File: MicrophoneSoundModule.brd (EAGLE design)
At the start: 22.9 x 17.8 mm, 23 parts, among them IC1 TLC272 TSSOP8

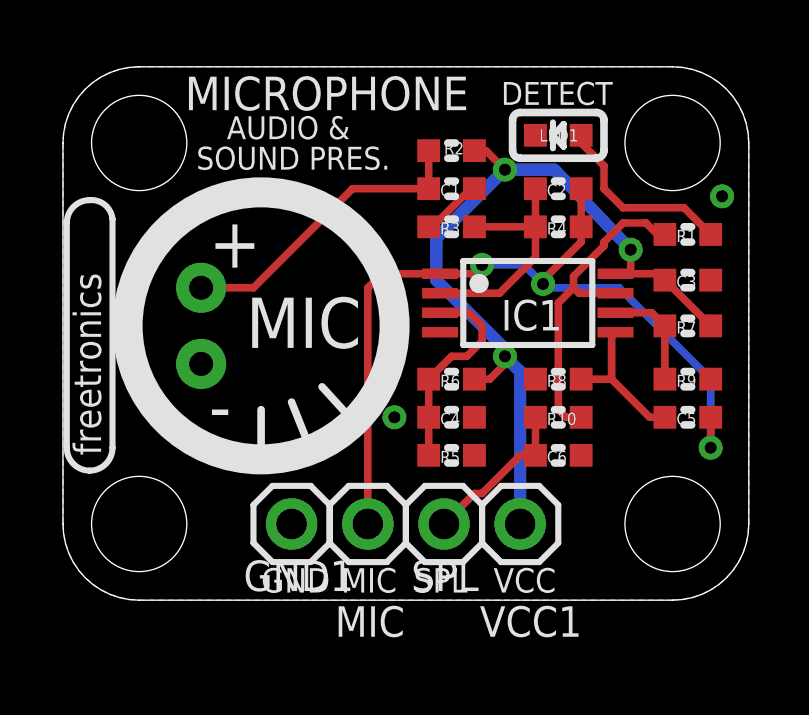
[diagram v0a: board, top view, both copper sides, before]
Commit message: Reorient AC decoupling capacitors to reduce noise
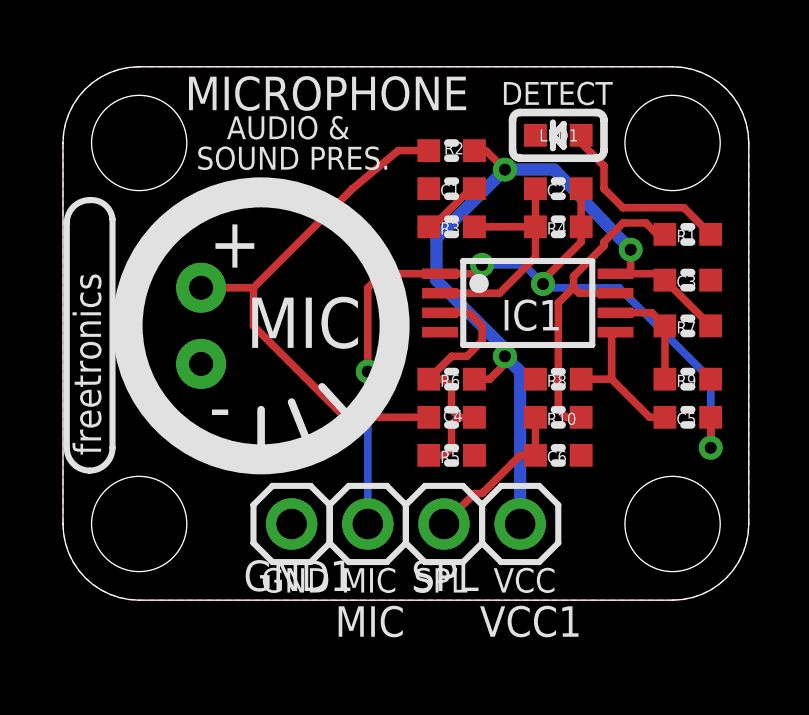
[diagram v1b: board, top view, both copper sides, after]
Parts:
- C4: value 1uF 10V -> 4.7uF 10V
- turned C4 to 0 degrees
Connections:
- net GND: now also C1.1; no longer C4.1
- net N$2: now also C4.1; no longer C1.1
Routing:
- net N$2: track 10.2 -> 17.8 mm
- net N$8: track 6.93 -> 8.88 mm
- net N$6: vias 3 -> 4
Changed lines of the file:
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@@
 <layer number="23" name="tOrigins" color="15" fill="1" visible="yes" active="yes"/>
 <layer number="24" name="bOrigins" color="15" fill="1" visible="yes" active="yes"/>
-<layer number="25" name="tNames" color="7" fill="1" visible="no" active="yes"/>
+<layer number="25" name="tNames" color="7" fill="1" visible="yes" active="yes"/>
 <layer number="26" name="bNames" color="7" fill="1" visible="no" active="yes"/>
 <layer number="27" name="tValues" color="7" fill="1" visible="no" active="yes"/>
@@
 <attribute name="VALUE" x="11.938" y="6.4008" size="0.4064" layer="27" font="vector"/>
 </element>
-<element name="C4" library="freetronics-master-v1" package="0603" value="1uF 10V" x="12.954" y="6.096" smashed="yes" rot="R180">
-<attribute name="NAME" x="12.573" y="5.842" size="0.4064" layer="25" font="vector"/>
-<attribute name="VALUE" x="13.97" y="7.0612" size="0.4064" layer="27" font="vector" rot="R180"/>
+<element name="C4" library="freetronics-master-v1" package="0603" value="4.7uF 10V" x="12.954" y="6.096" smashed="yes">
+<attribute name="NAME" x="13.335" y="6.35" size="0.4064" layer="25" font="vector" rot="R180"/>
+<attribute name="VALUE" x="11.938" y="5.1308" size="0.4064" layer="27" font="vector"/>
 </element>
 <element name="C5" library="freetronics-master-v1" package="0603" value="100nF" x="20.828" y="6.096" smashed="yes" rot="R180">
@@
 <contactref element="MIC1" pad="GND"/>
 <contactref element="R5" pad="1"/>
-<contactref element="C4" pad="1"/>
 <contactref element="R8" pad="1"/>
 <contactref element="R9" pad="1"/>
 <contactref element="C6" pad="1"/>
 <contactref element="GND1" pad="1"/>
-<via x="11.049" y="6.096" extent="1-16" drill="0.4"/>
-<via x="21.971" y="13.462" extent="1-16" drill="0.4"/>
 <polygon width="0.2032" layer="16" orphans="yes">
 <vertex x="2.54" y="17.78" curve="90"/>
@@
 <vertex x="2.54" y="17.78" curve="90"/>
 </polygon>
+<contactref element="C1" pad="1"/>
 </signal>
 <signal name="VCC">
@@
 <contactref element="IC1" pad="8"/>
 <contactref element="C3" pad="1"/>
-<contactref element="R6" pad="2"/>
 <contactref element="R7" pad="2"/>
 <contactref element="VCC1" pad="1"/>
@@
 <wire x1="14.732" y1="8.128" x2="14.732" y2="7.874" width="0.254" layer="1"/>
 <wire x1="14.732" y1="7.874" x2="14.224" y2="7.366" width="0.254" layer="1"/>
-<wire x1="14.224" y1="7.366" x2="13.716" y2="7.366" width="0.254" layer="1"/>
 <via x="18.923" y="11.684" extent="1-16" drill="0.4"/>
 <via x="14.732" y="14.351" extent="1-16" drill="0.4"/>
 <via x="14.732" y="8.128" extent="1-16" drill="0.4"/>
+<contactref element="R6" pad="2"/>
+<wire x1="14.224" y1="7.366" x2="13.716" y2="7.366" width="0.254" layer="1"/>
 </signal>
 <signal name="N$1">
@@
 <signal name="N$2">
 <contactref element="MIC1" pad="POS"/>
-<contactref element="C1" pad="1"/>
 <contactref element="R2" pad="1"/>
-<wire x1="12.192" y1="13.716" x2="12.192" y2="14.986" width="0.254" layer="1"/>
 <wire x1="4.604" y1="10.414" x2="6.35" y2="10.414" width="0.254" layer="1"/>
 <wire x1="6.35" y1="10.414" x2="9.652" y2="13.716" width="0.254" layer="1"/>
-<wire x1="9.652" y1="13.716" x2="12.192" y2="13.716" width="0.254" layer="1"/>
+<contactref element="C4" pad="1"/>
+<wire x1="9.652" y1="13.716" x2="11.176" y2="14.986" width="0.254" layer="1"/>
+<wire x1="11.176" y1="14.986" x2="12.192" y2="14.986" width="0.254" layer="1"/>
+<wire x1="12.192" y1="6.096" x2="9.398" y2="6.096" width="0.254" layer="1"/>
+<wire x1="9.398" y1="6.096" x2="6.35" y2="9.144" width="0.254" layer="1"/>
+<wire x1="6.35" y1="9.144" x2="6.35" y2="10.414" width="0.254" layer="1"/>
 </signal>
 <signal name="N$3">
@@
 <contactref element="C5" pad="1"/>
 <wire x1="17.272" y1="12.446" x2="17.272" y2="13.716" width="0.254" layer="1"/>
-<wire x1="10.16" y1="2.54" x2="10.16" y2="10.414" width="0.254" layer="1"/>
 <wire x1="10.16" y1="10.414" x2="10.627" y2="10.881" width="0.254" layer="1"/>
 <wire x1="10.627" y1="10.881" x2="12.569" y2="10.881" width="0.254" layer="1"/>
@@
 <via x="13.97" y="11.176" extent="1-16" drill="0.4"/>
 <via x="21.59" y="5.08" extent="1-16" drill="0.4"/>
-</signal>
-<signal name="N$5">
-<contactref element="R6" pad="1"/>
-<contactref element="R5" pad="2"/>
-<contactref element="C4" pad="2"/>
-<contactref element="IC1" pad="3"/>
-<wire x1="12.192" y1="4.826" x2="12.192" y2="6.096" width="0.254" layer="1"/>
-<wire x1="12.192" y1="6.096" x2="12.192" y2="7.366" width="0.254" layer="1"/>
-<wire x1="12.192" y1="7.366" x2="12.954" y2="8.128" width="0.254" layer="1"/>
-<wire x1="12.954" y1="8.128" x2="13.462" y2="8.128" width="0.254" layer="1"/>
-<wire x1="13.462" y1="8.128" x2="13.97" y2="8.636" width="0.254" layer="1"/>
-<wire x1="13.97" y1="8.636" x2="13.97" y2="9.144" width="0.254" layer="1"/>
-<wire x1="13.97" y1="9.144" x2="13.533" y2="9.581" width="0.254" layer="1"/>
-<wire x1="13.533" y1="9.581" x2="12.569" y2="9.581" width="0.254" layer="1"/>
+<wire x1="10.16" y1="2.54" x2="10.16" y2="7.62" width="0.254" layer="16"/>
+<via x="10.16" y="7.62" extent="1-16" drill="0.4"/>
+<wire x1="10.16" y1="7.62" x2="10.16" y2="10.414" width="0.254" layer="1"/>
 </signal>
 <signal name="N$7">
@@
 <wire x1="16.51" y1="9.906" x2="17.018" y2="10.414" width="0.254" layer="1"/>
 </signal>
+<signal name="N$8">
+<contactref element="R6" pad="1"/>
+<contactref element="R5" pad="2"/>
+<contactref element="C4" pad="2"/>
+<contactref element="IC1" pad="3"/>
+<wire x1="12.954" y1="8.128" x2="13.462" y2="8.128" width="0.254" layer="1"/>
+<wire x1="13.462" y1="8.128" x2="13.97" y2="8.636" width="0.254" layer="1"/>
+<wire x1="13.97" y1="8.636" x2="13.97" y2="9.144" width="0.254" layer="1"/>
+<wire x1="13.97" y1="9.144" x2="13.533" y2="9.581" width="0.254" layer="1"/>
+<wire x1="13.533" y1="9.581" x2="12.569" y2="9.581" width="0.254" layer="1"/>
+<wire x1="12.954" y1="8.128" x2="12.192" y2="7.366" width="0.254" layer="1"/>
+<wire x1="12.192" y1="7.366" x2="12.7" y2="7.366" width="0.254" layer="1"/>
+<wire x1="12.7" y1="7.366" x2="12.954" y2="7.112" width="0.254" layer="1"/>
+<wire x1="12.954" y1="7.112" x2="12.954" y2="6.35" width="0.254" layer="1"/>
+<wire x1="12.954" y1="6.35" x2="13.208" y2="6.096" width="0.254" layer="1"/>
+<wire x1="13.716" y1="6.096" x2="13.208" y2="6.096" width="0.254" layer="1"/>
+<wire x1="13.208" y1="6.096" x2="12.954" y2="5.842" width="0.254" layer="1"/>
+<wire x1="12.954" y1="5.842" x2="12.954" y2="5.08" width="0.254" layer="1"/>
+<wire x1="12.954" y1="5.08" x2="12.7" y2="4.826" width="0.254" layer="1"/>
+<wire x1="12.7" y1="4.826" x2="12.192" y2="4.826" width="0.254" layer="1"/>
+</signal>
 </signals>

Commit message: Bump revision, add revision to PCB, update schematic PDF
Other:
- board text added: "(C)2013 Freetronics Pty Ltd"
- board text added: "V1.1"
- board text removed: "(C)2011 Freetronics Pty Ltd"
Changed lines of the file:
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@@
 <setting verticaltext="up"/>
 </settings>
-<grid distance="0.01" unitdist="inch" unit="inch" style="lines" multiple="1" display="no" altdistance="0.005" altunitdist="inch" altunit="inch"/>
+<grid distance="0.01" unitdist="inch" unit="inch" style="lines" multiple="1" display="yes" altdistance="0.005" altunitdist="inch" altunit="inch"/>
 <layers>
 <layer number="1" name="Top" color="4" fill="1" visible="yes" active="yes"/>
@@
 <layer number="20" name="Dimension" color="15" fill="1" visible="yes" active="yes"/>
 <layer number="21" name="tPlace" color="16" fill="1" visible="yes" active="yes"/>
-<layer number="22" name="bPlace" color="14" fill="1" visible="yes" active="yes"/>
+<layer number="22" name="bPlace" color="6" fill="1" visible="yes" active="yes"/>
 <layer number="23" name="tOrigins" color="15" fill="1" visible="yes" active="yes"/>
 <layer number="24" name="bOrigins" color="15" fill="1" visible="yes" active="yes"/>
@@
 <text x="20.574" y="5.969" size="0.8636" layer="22" font="vector" ratio="15" rot="MR0">SKU: MIC</text>
 <text x="15.748" y="15.748" size="1.016" layer="22" font="vector" ratio="15" rot="MR0">freetronics</text>
-<text x="20.574" y="12.192" size="0.8128" layer="22" font="vector" ratio="17" rot="MR0">(C)2011 Freetronics Pty Ltd</text>
+<text x="20.574" y="12.192" size="0.8128" layer="22" font="vector" ratio="17" rot="MR0">(C)2013 Freetronics Pty Ltd</text>
 <text x="4.064" y="16.3322" size="1.1176" layer="21" font="vector" ratio="18">MICROPHONE</text>
 <text x="2.667" y="8.89" size="0.762" layer="22" font="vector" ratio="15" rot="MR0">2.7</text>
@@
 <hole x="2.54" y="15.24" drill="3.175"/>
 <hole x="20.32" y="15.24" drill="3.175"/>
+<text x="19.812" y="7.62" size="0.762" layer="22" font="vector" ratio="15" rot="MR0">V1.1</text>
 </plain>
 <attributes>
